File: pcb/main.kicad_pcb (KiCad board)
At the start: 2 copper layers, 127 x 122.2 mm, 109 parts, among them J1 Barrel_Jack, J2 NXC digit iface, J3 NXC num iface, J4 Conn_01x03, J5 ICSP, J6 Conn_02x06_Counter_Clockwise, J7 Conn_02x12_Counter_Clockwise, Q1 IRF740, Q10 ZVP1320F, Q11 BSS127S, Q12 ZVN3320F, Q13 BSS127S, Q14 BSS127S, Q15 ZVP1320F, Q16 BSS127S, Q17 BSS127S, Q18 ZVN3320F, Q19 BSS127S, Q2 ZVN3320F, Q20 ZVP1320F, Q3 BSS127S, Q4 ZVP1320F, Q5 BSS127S, Q6 BSS127S, Q7 ZVN3320F, Q8 BSS127S, Q9 BSS127S, SW1 Tactile SPST, SW2 Tactile SPST, SW3 Tactile SPST, U1 CD4028, U2 NCP1117, U3 PIC24FV32KA302-I_SO, U4 DS1307Z+, U5 MAX1771, Y1 8 MHz, Y2 32.768 kHz

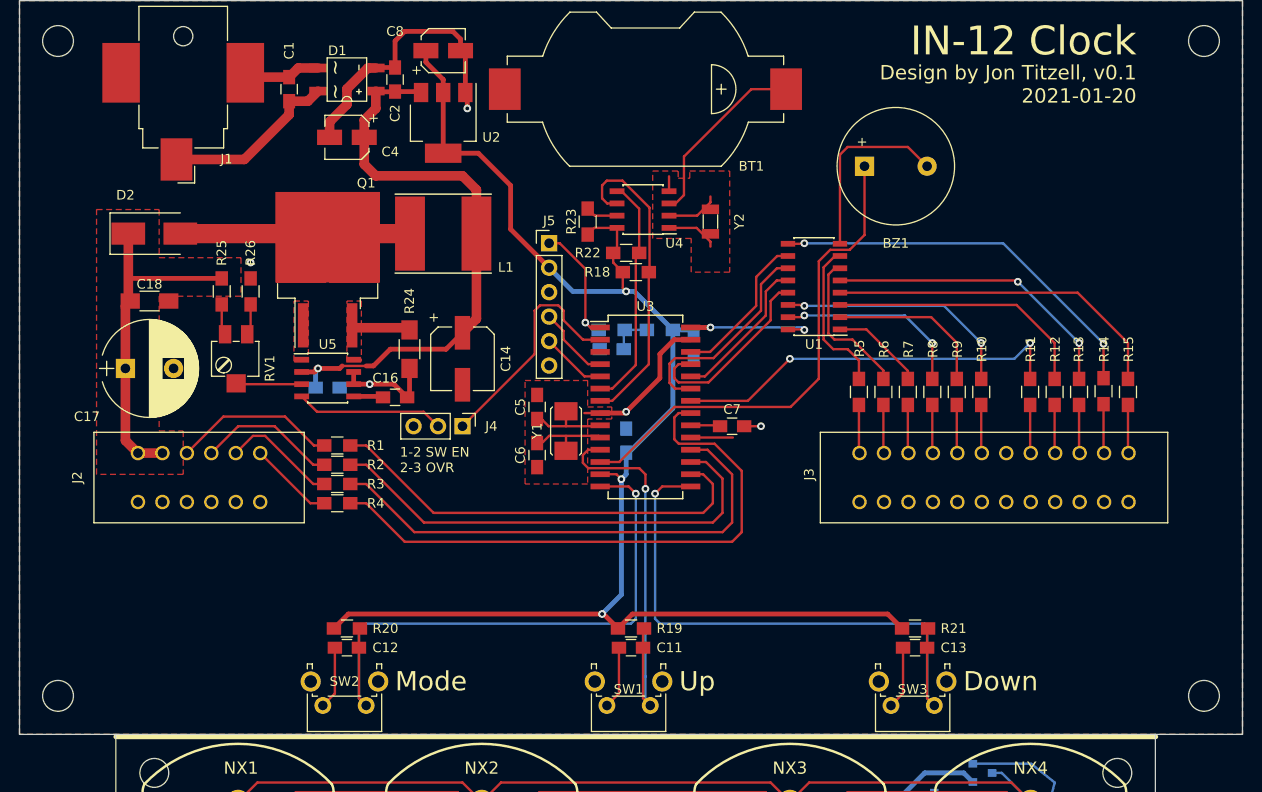
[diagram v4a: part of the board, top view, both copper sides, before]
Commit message: Update board to reflect new crystal and rectifier footprint. Update silkscreen ver/date, add new board renders and schematic plots.
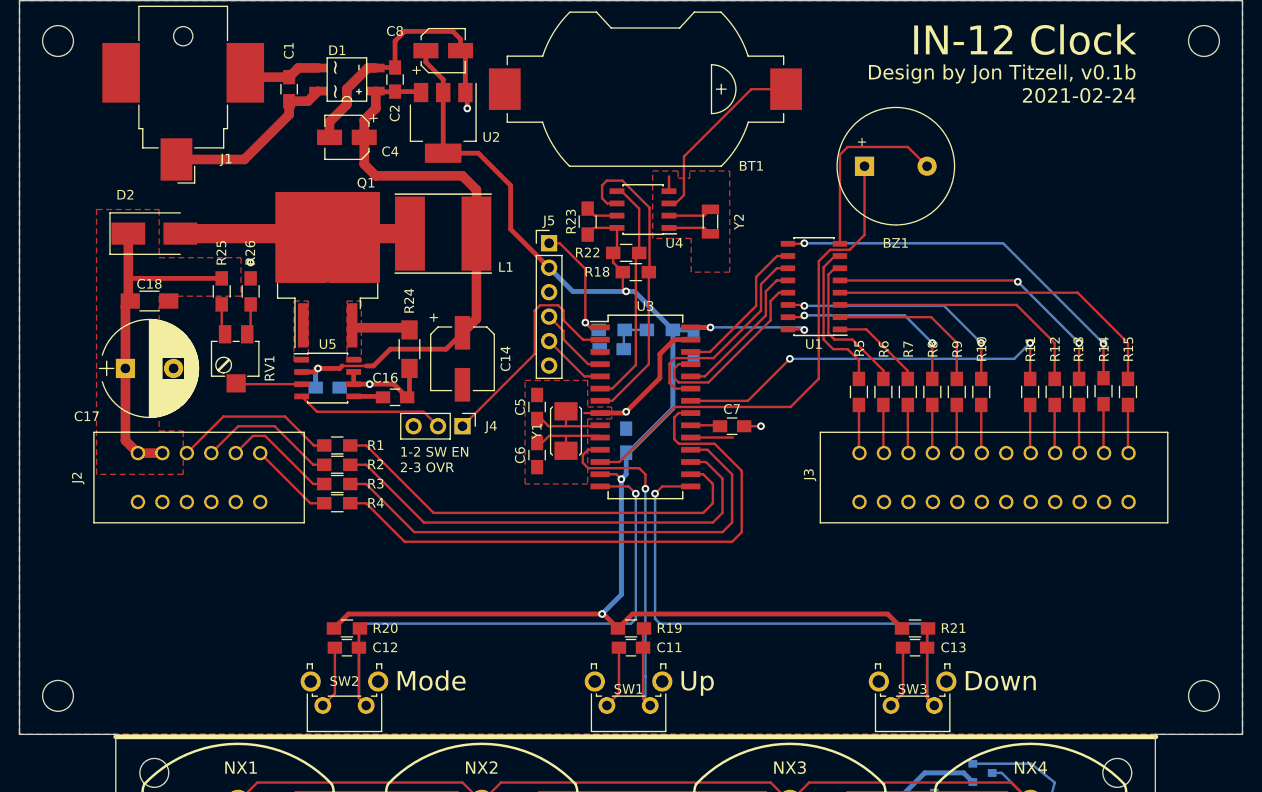
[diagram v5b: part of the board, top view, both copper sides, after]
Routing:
- net Net-(U4-Pad2): track 5.47 -> 4.57 mm
- net Net-(U4-Pad1): track 5.41 -> 4.56 mm
- net /OSCI: track 9.56 -> 9.01 mm
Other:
- board text added: "Design by Jon Titzell, v0.1b 2021-02-24"
- board text added: "IN-12 Clock submodule by Jon Titzell, v0.1b 2021-02-24"
- board text removed: "Design by Jon Titzell, v0.1 2021-01-20"
- board text removed: "IN-12 Clock submodule by Jon Titzell, v0.1 2021-01-20"
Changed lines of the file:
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@@
   (general
     (thickness 1.6)
-    (drawings 29)
-    (tracks 810)
+    (drawings 30)
+    (tracks 808)
     (zones 0)
     (modules 109)
@@
     )
   )
+  (gr_line (start 207.95 104) (end 217 104) (layer Edge.Cuts) (width 0.05))
   (gr_line (start 100 104.25) (end 208 104.25) (layer B.SilkS) (width 0.5))
   (gr_line (start 100 104.25) (end 208 104.25) (layer F.SilkS) (width 0.5))
-  (gr_line (start 90 104) (end 217 104) (layer Edge.Cuts) (width 0.05))
+  (gr_line (start 90 104) (end 100 104) (layer Edge.Cuts) (width 0.05))
   (gr_text Down (at 188 98.5) (layer F.SilkS)
     (effects (font (size 2 2) (thickness 0.3)) (justify left))
@@
     (effects (font (size 3 3) (thickness 0.5)) (justify right))
   )
-  (gr_text "Design by Jon Titzell, v0.1\n2021-01-20" (at 206 36.5) (layer F.SilkS)
+  (gr_text "Design by Jon Titzell, v0.1b\n2021-02-24" (at 206 36.5) (layer F.SilkS)
     (effects (font (size 1.5 1.5) (thickness 0.2)) (justify right))
   )
@@
   (gr_line (start 217 27.8) (end 90 27.8) (layer Margin) (width 0.15))
   (gr_line (start 217 150) (end 217 27.8) (layer Margin) (width 0.15))
-  (gr_text "IN-12 Clock submodule\nby Jon Titzell, v0.1\n2021-01-20" (at 154 109) (layer B.SilkS)
+  (gr_text "IN-12 Clock submodule\nby Jon Titzell, v0.1b\n2021-02-24" (at 154 109) (layer B.SilkS)
     (effects (font (size 0.8 0.8) (thickness 0.2)) (justify mirror))
   )
@@
   (segment (start 157.45 48.865) (end 158.135 48.865) (width 0.25) (layer F.Cu) (net 69))
   (segment (start 158.135 48.865) (end 159 48) (width 0.25) (layer F.Cu) (net 69))
-  (segment (start 161.75 48.75) (end 161.75 48.15) (width 0.25) (layer F.Cu) (net 70))
-  (segment (start 157.45 50.135) (end 160.365 50.135) (width 0.25) (layer F.Cu) (net 70))
-  (segment (start 160.365 50.135) (end 161.75 48.75) (width 0.25) (layer F.Cu) (net 70))
-  (segment (start 160.3175 51.405) (end 157.45 51.405) (width 0.25) (layer F.Cu) (net 71))
-  (segment (start 161.75 53.35) (end 161.75 52.8375) (width 0.25) (layer F.Cu) (net 71))
-  (segment (start 161.75 52.8375) (end 160.3175 51.405) (width 0.25) (layer F.Cu) (net 71))
+  (segment (start 157.45 50.135) (end 161.09 50.135) (width 0.25) (layer F.Cu) (net 70))
+  (segment (start 161.09 50.135) (end 161.75 49.475) (width 0.25) (layer F.Cu) (net 70))
+  (segment (start 161.13 51.405) (end 157.45 51.405) (width 0.25) (layer F.Cu) (net 71))
+  (segment (start 161.75 52.025) (end 161.13 51.405) (width 0.25) (layer F.Cu) (net 71))
   (segment (start 146.5 63.005) (end 146.5 62.12) (width 0.25) (layer F.Cu) (net 72))
   (segment (start 149.05 65.555) (end 146.5 63.005) (width 0.25) (layer F.Cu) (net 72))
@@
   (segment (start 159.7 71.905) (end 162.655 71.905) (width 0.25) (layer F.Cu) (net 85))
   (segment (start 150.3 71.905) (end 150.905 71.905) (width 0.25) (layer F.Cu) (net 86))
-  (segment (start 146.75 69.9) (end 146.75 72) (width 0.25) (layer F.Cu) (net 86))
   (segment (start 144.3 71.35) (end 143.75 71.35) (width 0.25) (layer F.Cu) (net 86))
   (segment (start 150.3 71.905) (end 150.205 72) (width 0.25) (layer F.Cu) (net 86))
   (segment (start 144.95 72) (end 144.3 71.35) (width 0.25) (layer F.Cu) (net 86))
   (segment (start 150.205 72) (end 144.95 72) (width 0.25) (layer F.Cu) (net 86))
-  (segment (start 146.75 75.1) (end 146.75 73) (width 0.25) (layer F.Cu) (net 87))
+  (segment (start 146.75 70.45) (end 146.75 72) (width 0.25) (layer F.Cu) (net 86))
   (segment (start 145 73) (end 144.35 73.65) (width 0.25) (layer F.Cu) (net 87))
   (segment (start 150.3 73.175) (end 150.125 73) (width 0.25) (layer F.Cu) (net 87))
   (segment (start 144.35 73.65) (end 143.75 73.65) (width 0.25) (layer F.Cu) (net 87))
   (segment (start 150.125 73) (end 145 73) (width 0.25) (layer F.Cu) (net 87))
+  (segment (start 146.75 75.1) (end 146.75 73) (width 0.25) (layer F.Cu) (net 87))
   (segment (start 155.15 62) (end 152.85 62) (width 0.25) (layer B.Cu) (net 88))
   (segment (start 152.75 62.1) (end 152.85 62) (width 0.25) (layer B.Cu) (net 88))
